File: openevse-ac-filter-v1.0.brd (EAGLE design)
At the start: 52.5 x 23 mm, 8 parts

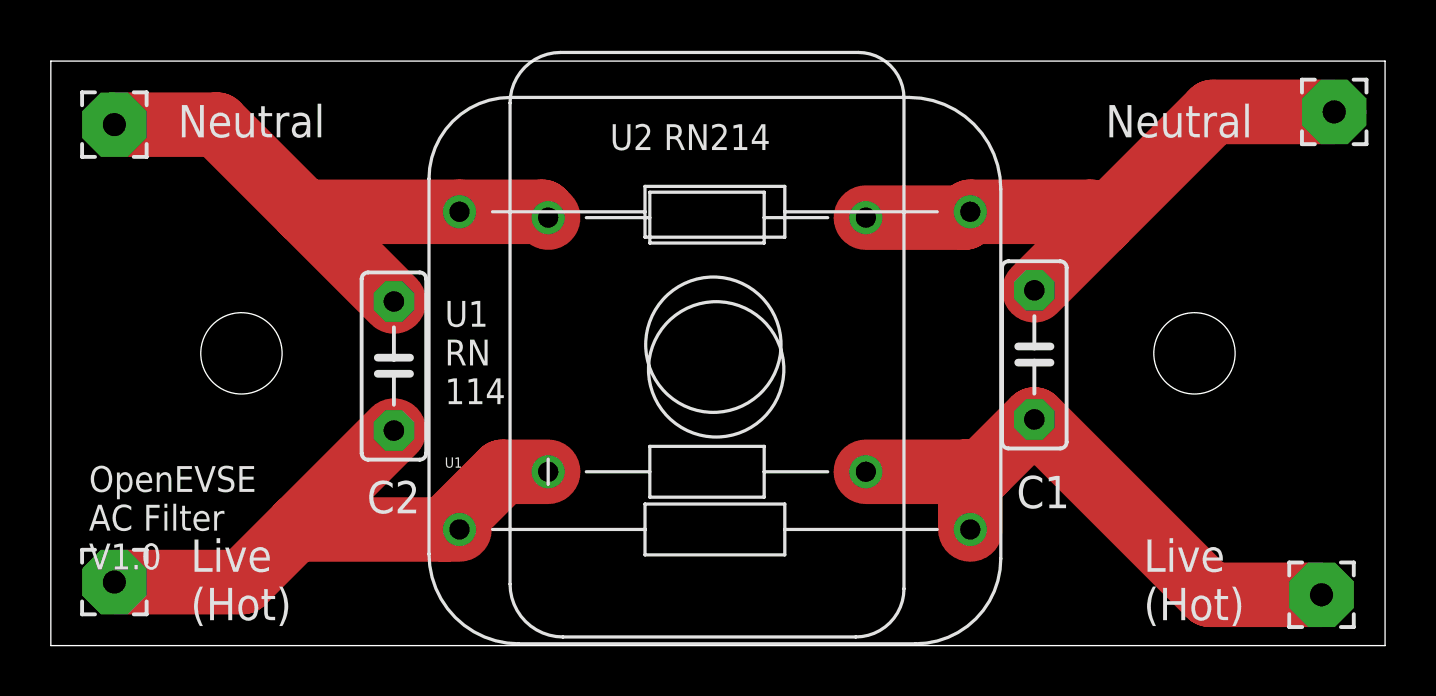
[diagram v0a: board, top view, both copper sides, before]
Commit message: V1.2 increase pad and hole size
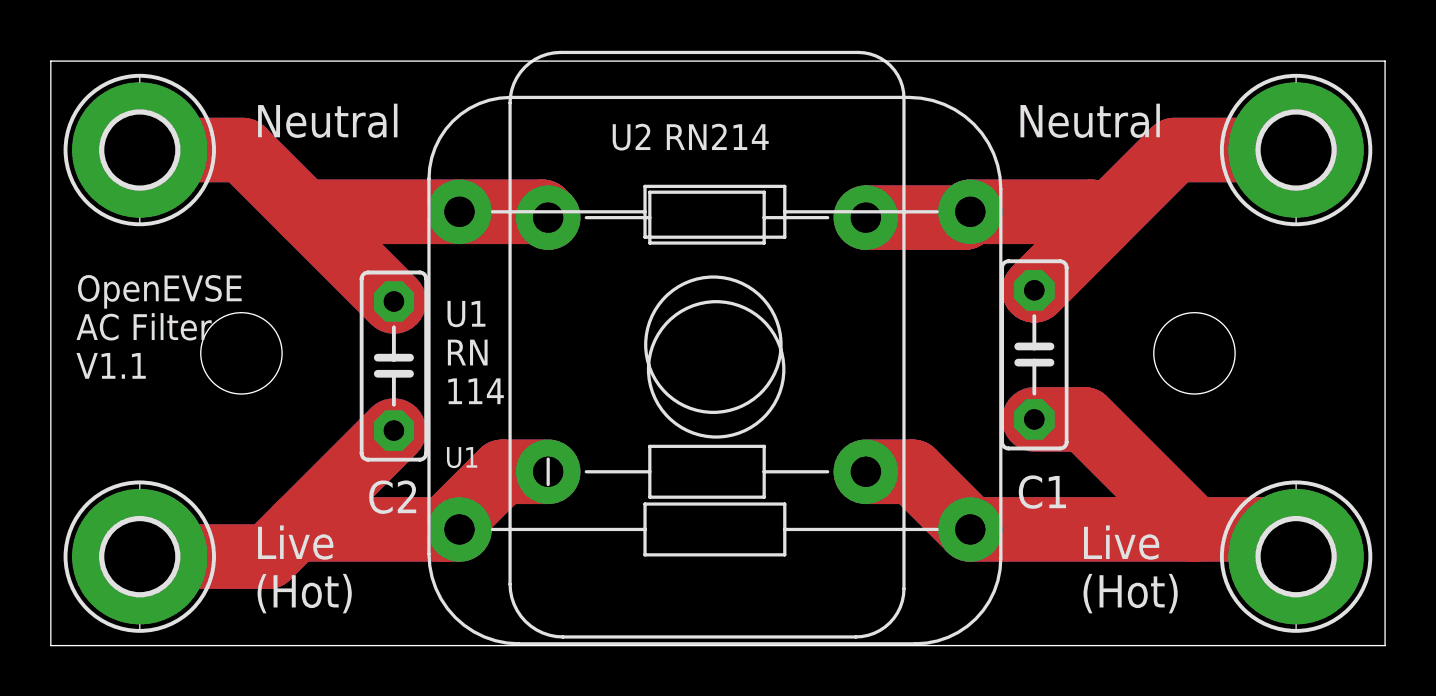
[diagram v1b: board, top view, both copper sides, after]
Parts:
- removed PAD1, PAD2, PAD3: (no value), wirepad:2,54/0,9
- removed PAD4: L, wirepad:2,54/0,9
- added H2, H3, H4, H5: MOUNT-PAD-ROUND2.8, holes:2,8-PAD
- C1: value (none) -> 10F
- C2: value (none) -> 10nF
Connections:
- net N$1: now also H5.B2,8; no longer PAD1.1
- net N$2: now also H2.B2,8; no longer PAD2.1
- net N$3: now also H3.B2,8; no longer PAD3.1
- net N$4: now also H4.B2,8; no longer PAD4.1
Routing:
- net N$5: track 0.00 -> 26.9 mm
- net N$7: track 0.00 -> 23.4 mm
- net N$8: track 0.00 -> 22.2 mm
- net N$6: track 0.00 -> 22.1 mm
- net N$1: track 24.0 -> 26.9 mm
- net N$2: track 24.3 -> 25.9 mm
- net N$4: track 23.6 -> 22.2 mm
- net N$3: track 24.9 -> 23.4 mm
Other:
- board text added: "OpenEVSE AC Filter V1.1"
- board text removed: "OpenEVSE AC Filter V1.0"
